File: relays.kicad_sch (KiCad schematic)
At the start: 15 parts, among them J3 relays, J4 relays, K1 G5V-1, K2 G5V-1, K3 G5V-1, K4 G5V-1, K5 G5V-1, K6 G5V-1, K7 G5V-1, K8 G5V-1, U2 PCF8574, U3 ULN2803A

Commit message: redone the switch connectors to accomodate a current sense print. Rearranged parts and updated silk texts to be 50% of their original size
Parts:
- renumbered C5 to C301, J3 to J301, J4 to J302, JP1 to JP301, JP2 to JP302, K1 to K301, K2 to K302, K3 to K303, K4 to K304, K5 to K305, K6 to K306, K7 to K307, K8 to K308, U2 to U301, U3 to U302
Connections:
- net at K306.10: now also J302.4 (Pin_4); no longer J302.3 (Pin_3)
- net at JP302.2 (B), K305.5, K305.6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: now also J302.1 (Pin_1); no longer J302.5 (Pin_5)
- net at K301.10: now also J301.4 (Pin_4); no longer J301.5 (Pin_5)
- net at JP301.2 (B), K301.5, K301.6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: now also J301.5 (Pin_5); no longer J301.1 (Pin_1)
- net at K304.10: now also J301.1 (Pin_1); no longer J301.2 (Pin_2)
- net at K303.10: now also J301.2 (Pin_2); no longer J301.3 (Pin_3)
- net at K302.10: now also J301.3 (Pin_3); no longer J301.4 (Pin_4)
- net at K308.10: now also J302.2 (Pin_2); no longer J302.1 (Pin_1)
- net at K305.10: now also J302.5 (Pin_5); no longer J302.4 (Pin_4)
- net at K307.10: now also J302.3 (Pin_3); no longer J302.2 (Pin_2)
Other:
- moved on the sheet: J301, J302

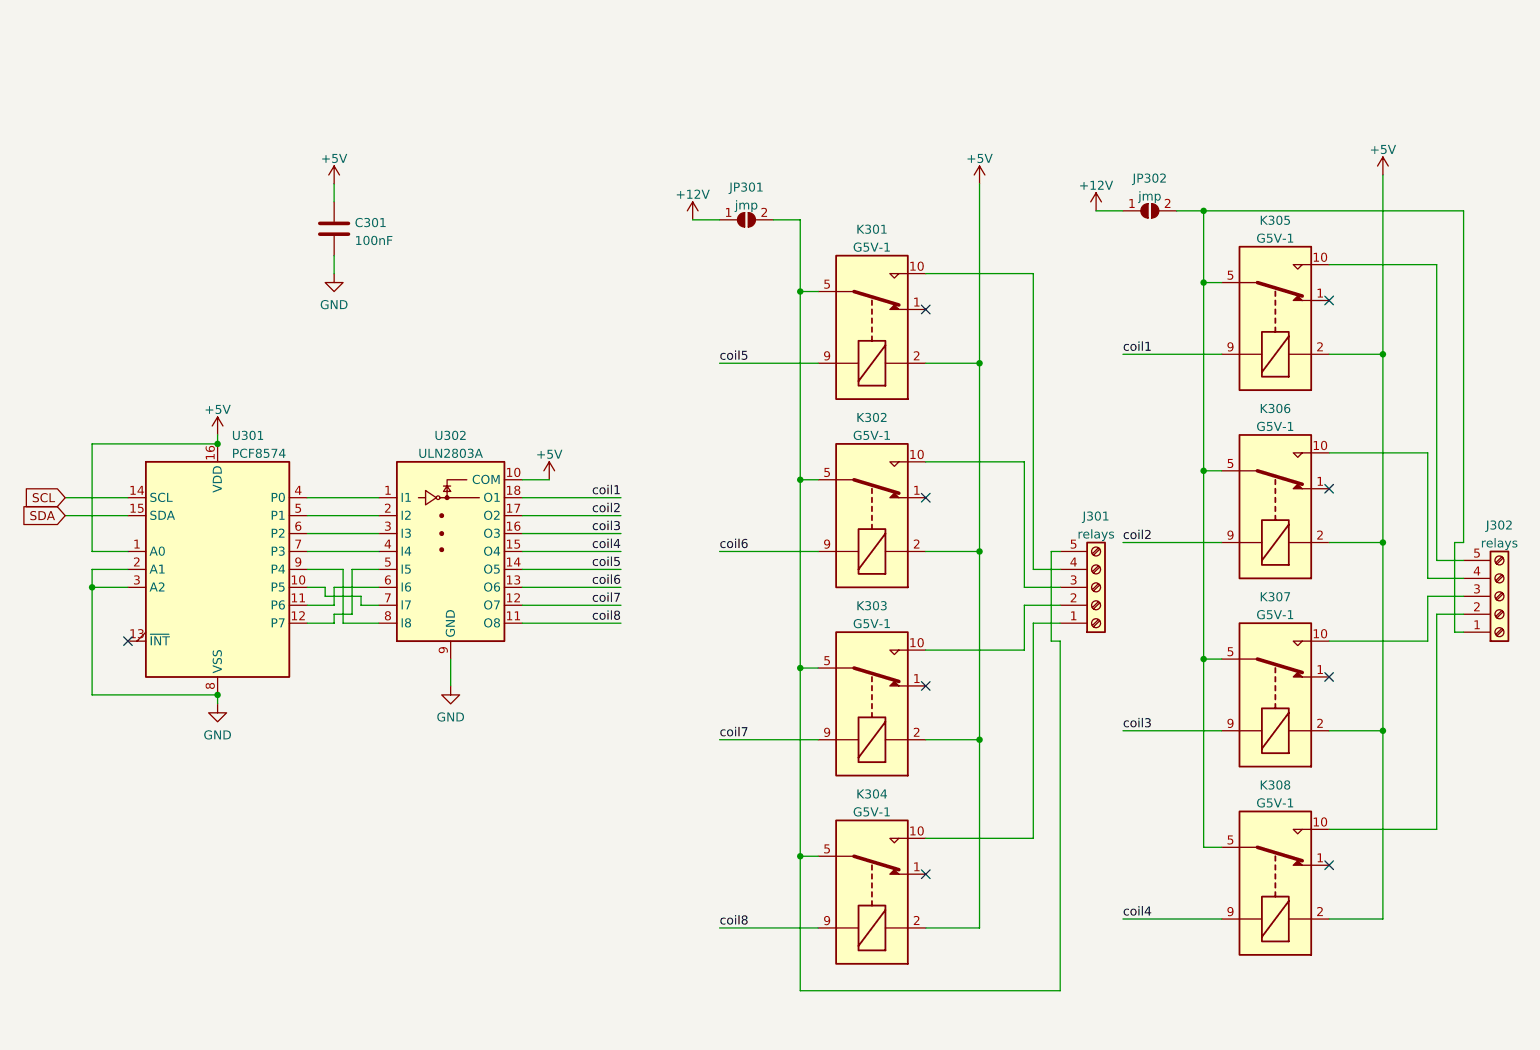
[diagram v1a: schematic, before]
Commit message: altered the code drastically and made a new PCB. PCB is still much work.
I finally fixed that issue where loco functions and speed were not serviced to the multimaus clients.
The Nx code also has been succesfully tested using the monitor.
MCP bug also has been solded. The bug was in assembleIO.py
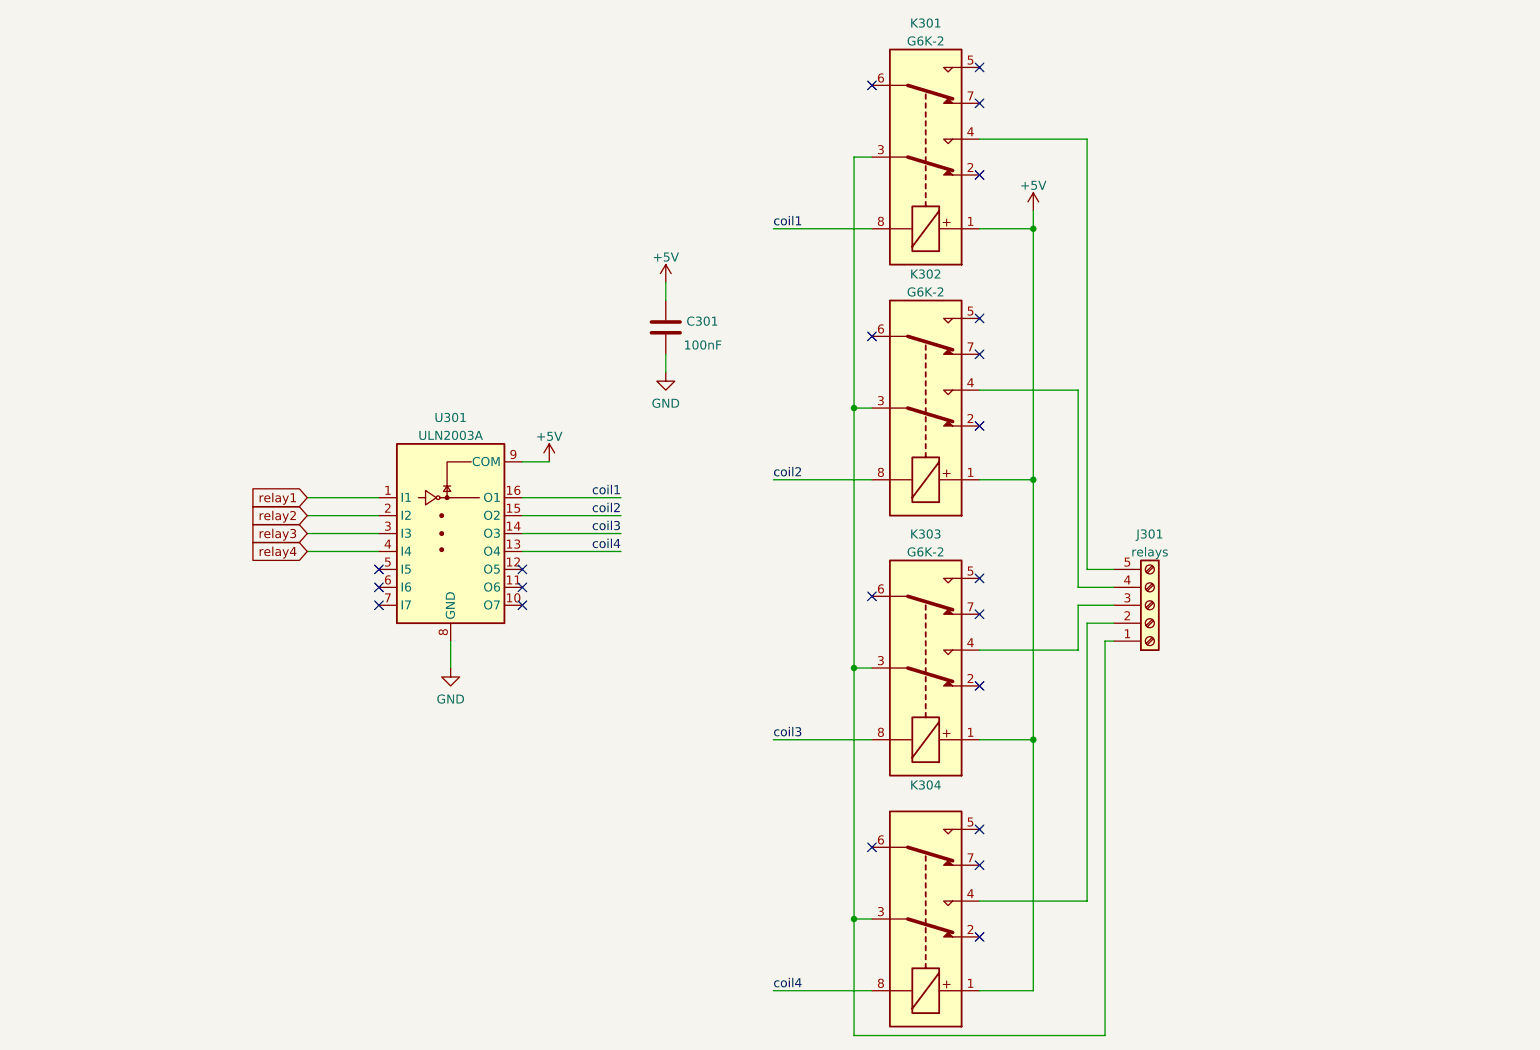
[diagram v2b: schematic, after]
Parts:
- removed J302: relays, TerminalBlock_Phoenix:TerminalBlock_Phoenix_MKDS-1,5-5-5.08_1x05_P5.08mm_Horizontal, symbol Connector:Screw_Terminal_01x05
- removed JP301, JP302: jmp, Jumper:SolderJumper-2_P1.3mm_Open_RoundedPad1.0x1.5mm, symbol Jumper:SolderJumper_2_Open
- removed K301, K302, K303, K304, K305, K306, K307, K308: G5V-1, Relay_THT:Relay_SPDT_Omron_G5V-1, symbol Relay:G5V-1
- removed U301: PCF8574, Package_DIP:DIP-16_W7.62mm_Socket, symbol Interface_Expansion:PCF8574
- removed U302: ULN2803A, Package_DIP:DIP-18_W7.62mm_Socket, symbol Transistor_Array:ULN2803A
- added K301, K302, K303: G6K-2, symbol Relay:G6K-2
- added K304: (no value), symbol Relay:G6K-2
- added U301: ULN2003A, symbol Transistor_Array:ULN2003A
- C301: footprint Capacitor_THT:C_Disc_D3.0mm_W1.6mm_P2.50mm -> Capacitor_SMD:C_0603_1608Metric_Pad1.08x0.95mm_HandSolder; JLCPCB Part# (none) -> C14663
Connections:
- net +5V: now also K301.1, K302.1, K303.1, K304.1, U301.9 (COM)
- net GND: now also U301.8 (GND)
- net coil1: now also K301.8, U301.16 (O1)
- net coil2: now also K302.8, U301.15 (O2)
- net coil3: now also K303.8, U301.14 (O3)
- net coil4: now also K304.8, U301.13 (O4)
- net at J301.4 (Pin_4): now also K302.4
- net at J301.5 (Pin_5): now also K301.4
- net at J301.1 (Pin_1): now also K301.3, K302.3, K303.3, K304.3
- net at J301.2 (Pin_2): now also K304.4
- net at J301.3 (Pin_3): now also K303.4
- new net relay1: U301.1 (I1)
- new net relay2: U301.2 (I2)
- new net relay3: U301.3 (I3)
- new net relay4: U301.4 (I4)
- no-connect marks 9 -> 22

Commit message: added missing schematics
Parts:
- K301, K302, K303: footprint (none) -> Relay_SMD:Relay_DPDT_Omron_G6K-2F-Y
- K304: value (none) -> G6K-2; footprint (none) -> Relay_SMD:Relay_DPDT_Omron_G6K-2F-Y
- U301: footprint (none) -> Package_SO:SOIC-16W_5.3x10.2mm_P1.27mm
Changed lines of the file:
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@@
     (property "Reference" "U301" (id 0) (at 96.52 68.6902 0))
     (property "Value" "ULN2003A" (id 1) (at 96.52 71.2271 0))
-    (property "Footprint" "" (id 2) (at 97.79 99.06 0)
+    (property "Footprint" "Package_SO:SOIC-16W_5.3x10.2mm_P1.27mm" (id 2) (at 97.79 99.06 0)
       (effects (font (size 1.27 1.27)) (justify left) hide)
     )
@@
     (in_bom yes) (on_board yes) (fields_autoplaced)
     (property "Reference" "K304" (id 0) (at 163.83 120.7602 90))
-    (property "Value" "" (id 1) (at 163.83 123.2971 90))
-    (property "Footprint" "" (id 2) (at 163.83 139.7 0)
+    (property "Value" "G6K-2" (id 1) (at 163.83 123.2971 90))
+    (property "Footprint" "Relay_SMD:Relay_DPDT_Omron_G6K-2F-Y" (id 2) (at 163.83 139.7 0)
       (effects (font (size 1.27 1.27)) (justify left) hide)
     )
@@
     (property "Reference" "K303" (id 0) (at 163.83 85.2002 90))
     (property "Value" "G6K-2" (id 1) (at 163.83 87.7371 90))
-    (property "Footprint" "" (id 2) (at 163.83 104.14 0)
+    (property "Footprint" "Relay_SMD:Relay_DPDT_Omron_G6K-2F-Y" (id 2) (at 163.83 104.14 0)
       (effects (font (size 1.27 1.27)) (justify left) hide)
     )
@@
     (property "Reference" "K302" (id 0) (at 163.83 48.3702 90))
     (property "Value" "G6K-2" (id 1) (at 163.83 50.9071 90))
-    (property "Footprint" "" (id 2) (at 163.83 67.31 0)
+    (property "Footprint" "Relay_SMD:Relay_DPDT_Omron_G6K-2F-Y" (id 2) (at 163.83 67.31 0)
       (effects (font (size 1.27 1.27)) (justify left) hide)
     )
@@
     (property "Reference" "K301" (id 0) (at 163.83 12.8102 90))
     (property "Value" "G6K-2" (id 1) (at 163.83 15.3471 90))
-    (property "Footprint" "" (id 2) (at 163.83 31.75 0)
+    (property "Footprint" "Relay_SMD:Relay_DPDT_Omron_G6K-2F-Y" (id 2) (at 163.83 31.75 0)
       (effects (font (size 1.27 1.27)) (justify left) hide)
     )
